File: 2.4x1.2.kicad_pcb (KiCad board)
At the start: 2 copper layers, 12 x 23.2 mm, 18 parts, among them J1 Conn_01x08, J2 Conn_01x08

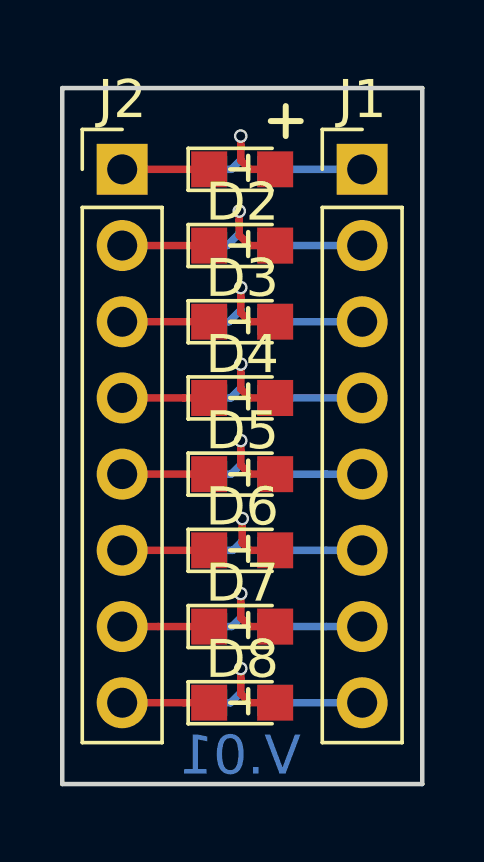
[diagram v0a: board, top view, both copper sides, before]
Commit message: added size,gerber file and drill hole
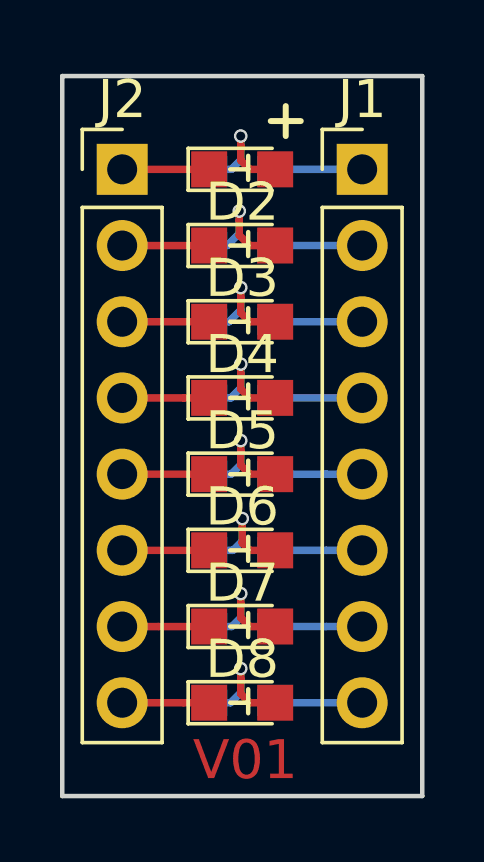
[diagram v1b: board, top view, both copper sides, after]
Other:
- board size 12 x 23.2 mm -> 12 x 24 mm
- board text added: "V01"
- board text removed: "V.01"
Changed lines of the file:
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@@
     (links 24)
     (no_connects 0)
-    (area 158.450001 106.3 180.2 133.8525)
+    (area 158.874999 109.924999 171.025001 134.075001)
     (thickness 1.6)
     (drawings 9)
@@
     (visible_elements 7FFFFFFF)
     (pcbplotparams
-      (layerselection 0x0ffff_80000001)
+      (layerselection 0x00030_80000001)
       (usegerberextensions false)
       (excludeedgelayer true)
@@
       (outputformat 1)
       (mirror false)
-      (drillshape 0)
+      (drillshape 1)
       (scaleselection 1)
-      (outputdirectory gerber/))
+      (outputdirectory ""))
   )
   (net 0 "")
@@
     )
   )
-  (dimension 23.2 (width 0.3) (layer Eco1.User)
-    (gr_text "23.200 mm" (at 173.7 122 270) (layer Eco1.User)
-      (effects (font (size 1.5 1.5) (thickness 0.3)))
-    )
-    (feature1 (pts (xy 170.95 133.6) (xy 175.05 133.6)))
-    (feature2 (pts (xy 170.95 110.4) (xy 175.05 110.4)))
-    (crossbar (pts (xy 172.35 110.4) (xy 172.35 133.6)))
-    (arrow1a (pts (xy 172.35 133.6) (xy 171.763579 132.473496)))
-    (arrow1b (pts (xy 172.35 133.6) (xy 172.936421 132.473496)))
-    (arrow2a (pts (xy 172.35 110.4) (xy 171.763579 111.526504)))
-    (arrow2b (pts (xy 172.35 110.4) (xy 172.936421 111.526504)))
-  )
-  (dimension 12 (width 0.3) (layer Eco1.User)
-    (gr_text "12.000 mm" (at 164.95 107.65) (layer Eco1.User)
-      (effects (font (size 1.5 1.5) (thickness 0.3)))
-    )
-    (feature1 (pts (xy 170.95 110.4) (xy 170.95 106.3)))
-    (feature2 (pts (xy 158.95 110.4) (xy 158.95 106.3)))
-    (crossbar (pts (xy 158.95 109) (xy 170.95 109)))
-    (arrow1a (pts (xy 170.95 109) (xy 169.823496 109.586421)))
-    (arrow1b (pts (xy 170.95 109) (xy 169.823496 108.413579)))
-    (arrow2a (pts (xy 158.95 109) (xy 160.076504 109.586421)))
-    (arrow2b (pts (xy 158.95 109) (xy 160.076504 108.413579)))
-  )
-  (gr_text V.01 (at 164.875 132.65) (layer B.Cu)
-    (effects (font (size 1.3 1.3) (thickness 0.325)) (justify mirror))
+  (gr_text V01 (at 165.05 132.8) (layer F.Cu)
+    (effects (font (size 1.3 1.3) (thickness 0.325)))
   )
   (gr_line (start 166.9 111.5) (end 165.9 111.5) (layer F.SilkS) (width 0.2))
   (gr_line (start 166.4 112) (end 166.4 111) (layer F.SilkS) (width 0.2))
-  (gr_line (start 158.95 133.6) (end 158.95 110.4) (layer Edge.Cuts) (width 0.15))
-  (gr_line (start 170.95 133.6) (end 158.95 133.6) (layer Edge.Cuts) (width 0.15))
-  (gr_line (start 170.95 110.4) (end 170.95 133.6) (layer Edge.Cuts) (width 0.15))
-  (gr_line (start 158.95 110.4) (end 170.95 110.4) (layer Edge.Cuts) (width 0.15))
+  (dimension 24 (width 0.3) (layer F.SilkS)
+    (gr_text "24.000 mm" (at 173.45 122 270) (layer F.SilkS)
+      (effects (font (size 1.5 1.5) (thickness 0.3)))
+    )
+    (feature1 (pts (xy 170.95 134) (xy 174.8 134)))
+    (feature2 (pts (xy 170.95 110) (xy 174.8 110)))
+    (crossbar (pts (xy 172.1 110) (xy 172.1 134)))
+    (arrow1a (pts (xy 172.1 134) (xy 171.513579 132.873496)))
+    (arrow1b (pts (xy 172.1 134) (xy 172.686421 132.873496)))
+    (arrow2a (pts (xy 172.1 110) (xy 171.513579 111.126504)))
+    (arrow2b (pts (xy 172.1 110) (xy 172.686421 111.126504)))
+  )
+  (dimension 12 (width 0.3) (layer F.SilkS)
+    (gr_text "12.000 mm" (at 164.95 107.85) (layer F.SilkS)
+      (effects (font (size 1.5 1.5) (thickness 0.3)))
+    )
+    (feature1 (pts (xy 170.95 110) (xy 170.95 106.5)))
+    (feature2 (pts (xy 158.95 110) (xy 158.95 106.5)))
+    (crossbar (pts (xy 158.95 109.2) (xy 170.95 109.2)))
+    (arrow1a (pts (xy 170.95 109.2) (xy 169.823496 109.786421)))
+    (arrow1b (pts (xy 170.95 109.2) (xy 169.823496 108.613579)))
+    (arrow2a (pts (xy 158.95 109.2) (xy 160.076504 109.786421)))
+    (arrow2b (pts (xy 158.95 109.2) (xy 160.076504 108.613579)))
+  )
+  (gr_line (start 158.95 134) (end 158.95 110) (layer Edge.Cuts) (width 0.15))
+  (gr_line (start 170.95 134) (end 158.95 134) (layer Edge.Cuts) (width 0.15))
+  (gr_line (start 170.95 110) (end 170.95 134) (layer Edge.Cuts) (width 0.15))
+  (gr_line (start 158.95 110) (end 170.95 110) (layer Edge.Cuts) (width 0.15))
   (segment (start 164.1976 113.1092) (end 164.5908 113.1092) (width 0.25) (layer B.Cu) (net 1))
   (segment (start 164.5908 113.1092) (end 164.9 112.8) (width 0.25) (layer B.Cu) (net 1))
@@
     (polygon
       (pts
-        (xy 158.95 110.4) (xy 170.95 110.4) (xy 170.95 133.6) (xy 158.95 133.6)
+        (xy 158.95 110) (xy 170.95 110) (xy 170.95 134) (xy 158.95 134)
       )
     )
@@
     (polygon
       (pts
-        (xy 158.95 110.4) (xy 170.95 110.4) (xy 170.95 133.6) (xy 158.95 133.6)
+        (xy 158.95 110) (xy 170.95 110) (xy 170.95 134) (xy 158.95 134)
       )
     )
